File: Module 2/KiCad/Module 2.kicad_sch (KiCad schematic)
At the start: 15 parts

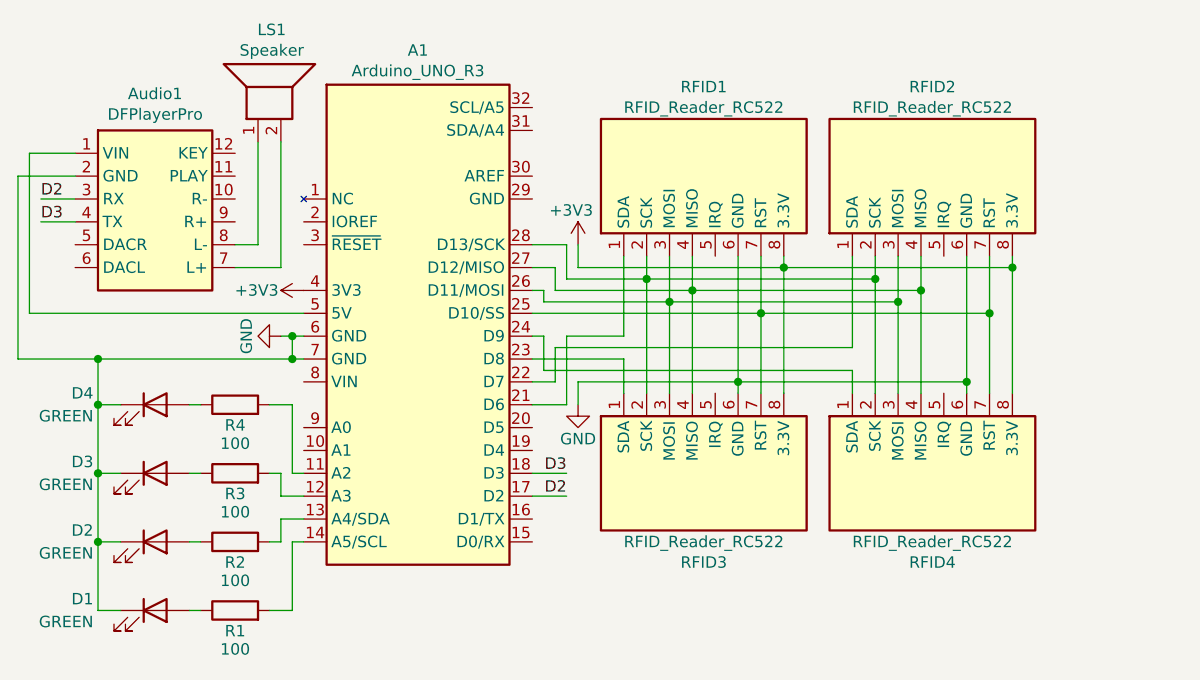
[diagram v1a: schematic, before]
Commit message: Updated Module 2 schematic
Also added .history folder to gitignore. This folder is an internal git repo created inside KiCad project folders independent from the automatic zip backups, if this is turned off, backups are also turned off. This might be a bug.
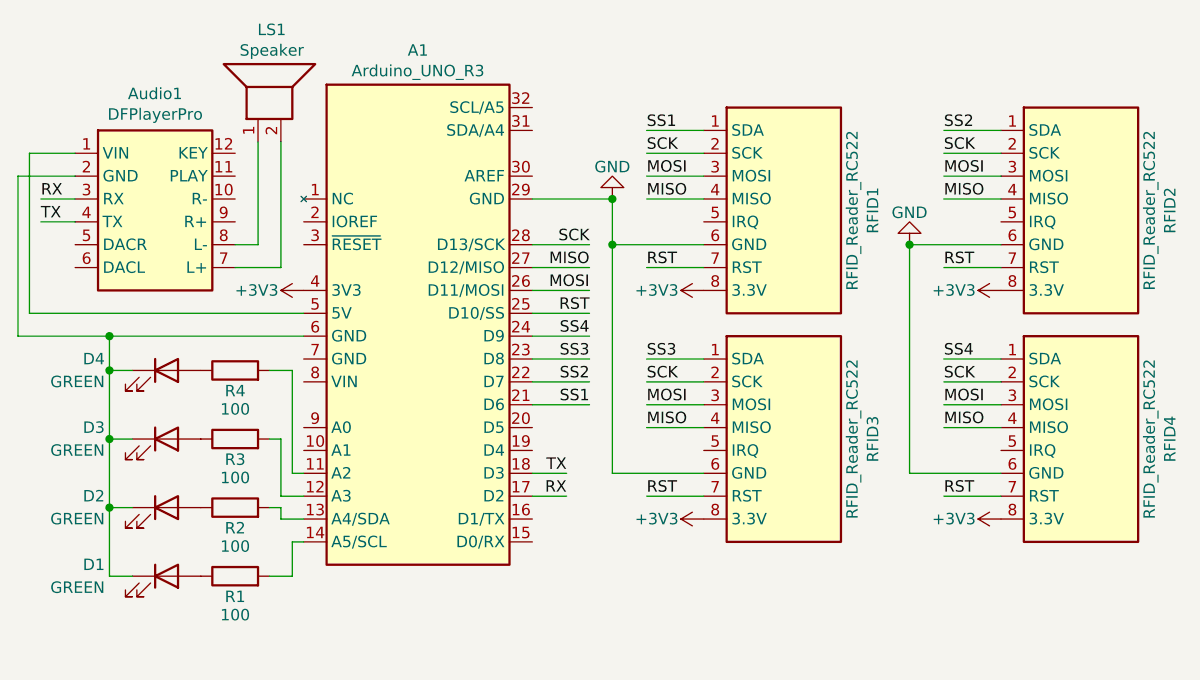
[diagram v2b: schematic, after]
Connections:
- net GND: now also A1.29 (GND); no longer A1.6 (GND), A1.7 (GND), Audio1.2 (GND), D1.1 (K), D2.1 (K), D3.1 (K), D4.1 (K)
- net SS1: now reaches A1.21 (D6), RFID1.1 (SDA)
- net SCK: now reaches A1.28 (D13/SCK), RFID1.2 (SCK), RFID2.2 (SCK), RFID3.2 (SCK), RFID4.2 (SCK)
- net MOSI: now reaches A1.26 (D11/MOSI), RFID1.3 (MOSI), RFID2.3 (MOSI), RFID3.3 (MOSI), RFID4.3 (MOSI)
- net MISO: now reaches A1.27 (D12/MISO), RFID1.4 (MISO), RFID2.4 (MISO), RFID3.4 (MISO), RFID4.4 (MISO)
- net RST: now reaches A1.25 (D10/SS), RFID1.7 (RST), RFID2.7 (RST), RFID3.7 (RST), RFID4.7 (RST)
- net SS4: now reaches A1.24 (D9), RFID4.1 (SDA)
- net SS3: now reaches A1.23 (D8), RFID3.1 (SDA)
- net SS2: now reaches A1.22 (D7), RFID2.1 (SDA)
- net D2 renamed RX
- net D3 renamed TX
- new net: A1.6 (GND), Audio1.2 (GND), D1.1 (K), D2.1 (K), D3.1 (K), D4.1 (K)
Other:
- moved on the sheet: D1, D2, D3, D4, R1, R2, R3, R4, RFID1, RFID2, RFID3, RFID4
